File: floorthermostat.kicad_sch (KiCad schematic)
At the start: 29 parts, among them J1 Temp sensor socket 3 pin, J2 spi7segdisp, J3 Conn_01x06_Socket, J5 Programmin connector, Q1 BC549, SW1 Reset pushbutton, SW2 Enable pushbutton, U1 ESP32-WROOM-32, U2 GOLD 240V 3A SSR, U3 BD33FC0FP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

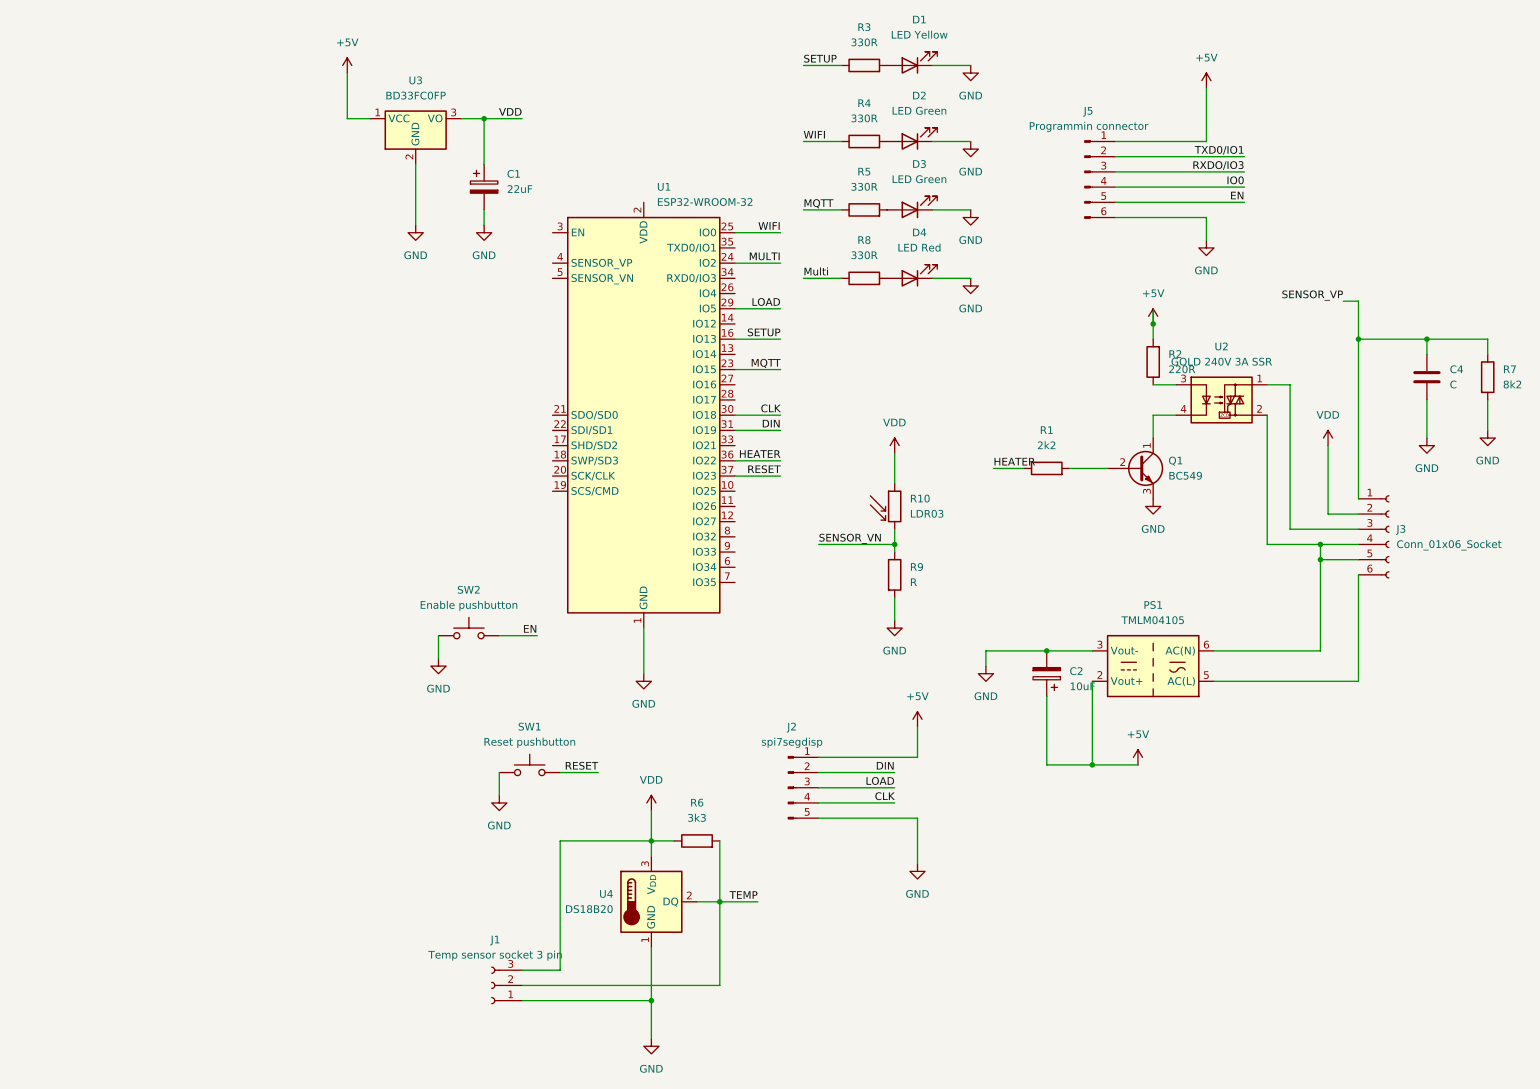
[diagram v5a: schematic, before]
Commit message: Checked all the component footprints.
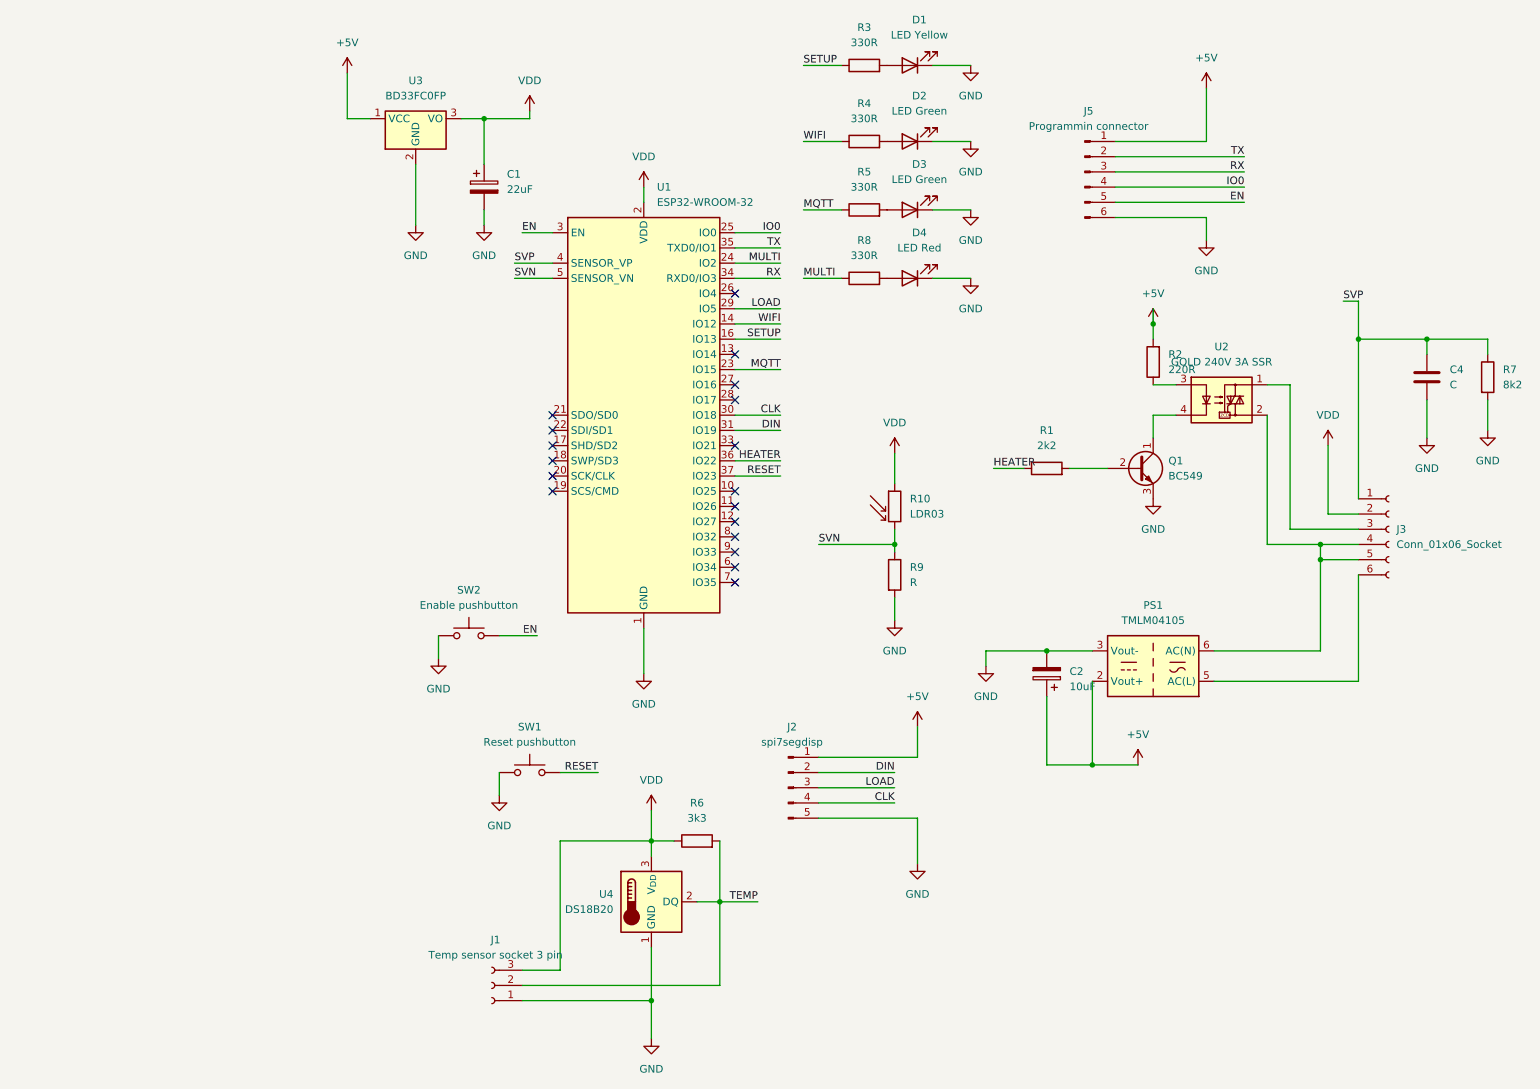
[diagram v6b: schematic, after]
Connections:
- net Multi is gone; now on net MULTI: R8.1
- net RXDO/IO3 is gone; now on net RX: J5.3 (Pin_3)
- net SENSOR_VN is gone; now on net SVN: R10.2, R9.1
- net SENSOR_VP is gone; now on net SVP: C4.1, J3.1 (Pin_1), R7.1
- net TXD0/IO1 is gone; now on net TX: J5.2 (Pin_2)
- net EN: now also U1.3 (EN)
- net IO0: now also U1.25 (IO0)
- net VDD: now also U1.2 (VDD)
- net WIFI: now also U1.14 (IO12); no longer U1.25 (IO0)
- net RX: now reaches U1.34 (RXD0/IO3)
- net TX: now reaches U1.35 (TXD0/IO1)
- net SVP: now reaches U1.4 (SENSOR_VP)
- net SVN: now reaches U1.5 (SENSOR_VN)
- no-connect marks 0 -> 18

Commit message: Started designing the pcb.
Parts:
- R2, R3, R4, R5, R6, R7, R8, R9: footprint Resistor_THT:R_Axial_DIN0207_L6.3mm_D2.5mm_P2.54mm_Vertical -> Resistor_THT:R_Axial_DIN0207_L6.3mm_D2.5mm_P15.24mm_Horizontal
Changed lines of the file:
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@@
 			)
 		)
-		(property "Footprint" "Resistor_THT:R_Axial_DIN0207_L6.3mm_D2.5mm_P2.54mm_Vertical"
+		(property "Footprint" "Resistor_THT:R_Axial_DIN0207_L6.3mm_D2.5mm_P15.24mm_Horizontal"
 			(at 149.86 23.368 90)
 			(effects
@@
 			)
 		)
-		(property "Footprint" "Resistor_THT:R_Axial_DIN0207_L6.3mm_D2.5mm_P2.54mm_Vertical"
+		(property "Footprint" "Resistor_THT:R_Axial_DIN0207_L6.3mm_D2.5mm_P15.24mm_Horizontal"
 			(at 149.86 58.928 90)
 			(effects
@@
 			)
 		)
-		(property "Footprint" "Resistor_THT:R_Axial_DIN0207_L6.3mm_D2.5mm_P2.54mm_Vertical"
+		(property "Footprint" "Resistor_THT:R_Axial_DIN0207_L6.3mm_D2.5mm_P15.24mm_Horizontal"
 			(at 252.222 73.66 90)
 			(effects
@@
 			)
 		)
-		(property "Footprint" "Resistor_THT:R_Axial_DIN0207_L6.3mm_D2.5mm_P2.54mm_Vertical"
+		(property "Footprint" "Resistor_THT:R_Axial_DIN0207_L6.3mm_D2.5mm_P15.24mm_Horizontal"
 			(at 149.86 47.498 90)
 			(effects
@@
 			)
 		)
-		(property "Footprint" "Resistor_THT:R_Axial_DIN0207_L6.3mm_D2.5mm_P2.54mm_Vertical"
+		(property "Footprint" "Resistor_THT:R_Axial_DIN0207_L6.3mm_D2.5mm_P15.24mm_Horizontal"
 			(at 199.898 71.12 90)
 			(effects
@@
 			)
 		)
-		(property "Footprint" "Resistor_THT:R_Axial_DIN0207_L6.3mm_D2.5mm_P2.54mm_Vertical"
+		(property "Footprint" "Resistor_THT:R_Axial_DIN0207_L6.3mm_D2.5mm_P15.24mm_Horizontal"
 			(at 121.92 152.908 90)
 			(effects
@@
 			)
 		)
-		(property "Footprint" "Resistor_THT:R_Axial_DIN0207_L6.3mm_D2.5mm_P2.54mm_Vertical"
+		(property "Footprint" "Resistor_THT:R_Axial_DIN0207_L6.3mm_D2.5mm_P15.24mm_Horizontal"
 			(at 153.162 106.68 90)
 			(effects
@@
 			)
 		)
-		(property "Footprint" "Resistor_THT:R_Axial_DIN0207_L6.3mm_D2.5mm_P2.54mm_Vertical"
+		(property "Footprint" "Resistor_THT:R_Axial_DIN0207_L6.3mm_D2.5mm_P15.24mm_Horizontal"
 			(at 149.86 36.068 90)
 			(effects

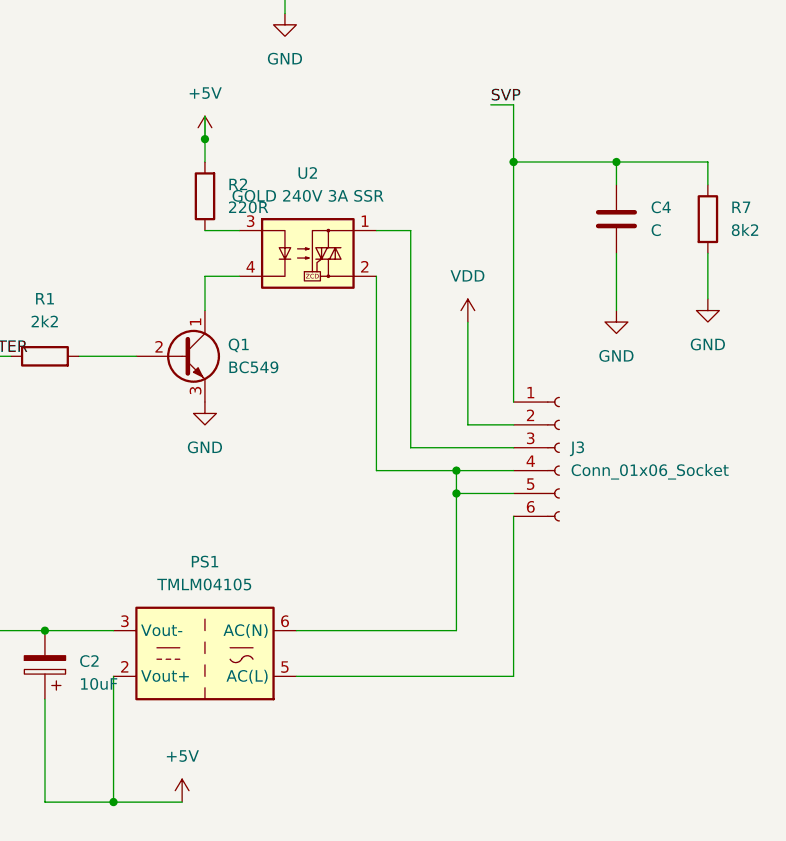
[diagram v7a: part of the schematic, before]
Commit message: Sketching component positions to pcb.
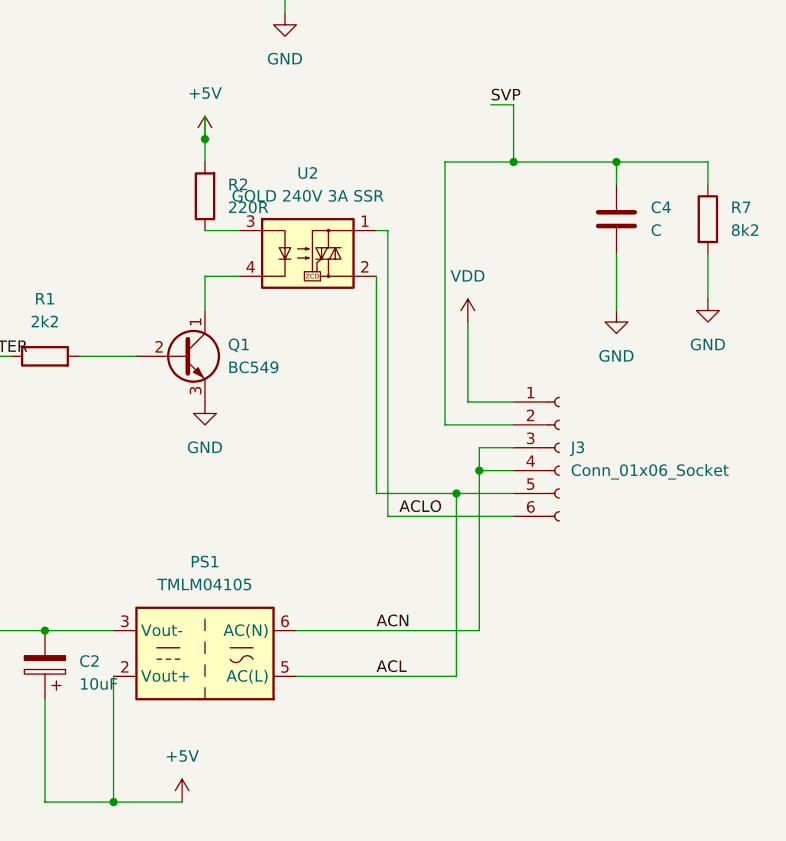
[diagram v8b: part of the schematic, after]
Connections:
- net SVP: now also J3.2 (Pin_2); no longer J3.1 (Pin_1)
- net VDD: now also J3.1 (Pin_1); no longer J3.2 (Pin_2)
- net ACLO: now reaches U2.1
- net ACLO: now also J3.6 (Pin_6); no longer J3.3 (Pin_3)
- net ACL: now reaches J3.5 (Pin_5), U2.2
- net ACL: now also PS1.5 (AC(L)); no longer J3.4 (Pin_4), PS1.6 (AC(N))
- new net ACN: J3.3 (Pin_3), J3.4 (Pin_4), PS1.6 (AC(N))
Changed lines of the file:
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@@
 	(paper "A4")
+	(junction
+		(at 114.3 177.8)
+		(diameter 0)
+		(color 0 0 0 0)
+	)
+	(junction
+		(at 86.36 30.48)
+		(diameter 0)
+		(color 0 0 0 0)
+	)
 	(junction
 		(at 232.41 67.31)
@@
 	)
 	(junction
-		(at 114.3 177.8)
+		(at 114.3 151.13)
+		(diameter 0)
+		(color 0 0 0 0)
+	)
+	(junction
+		(at 198.12 64.77)
+		(diameter 0)
+		(color 0 0 0 0)
+	)
+	(junction
+		(at 125.73 161.29)
 		(diameter 0)
 		(color 0 0 0 0)
@@
 	)
 	(junction
-		(at 86.36 30.48)
-		(diameter 0)
-		(color 0 0 0 0)
-	)
-	(junction
-		(at 114.3 151.13)
-		(diameter 0)
-		(color 0 0 0 0)
-	)
-	(junction
-		(at 226.06 101.6)
-		(diameter 0)
-		(color 0 0 0 0)
-	)
-	(junction
-		(at 198.12 64.77)
-		(diameter 0)
-		(color 0 0 0 0)
-	)
-	(junction
-		(at 125.73 161.29)
-		(diameter 0)
-		(color 0 0 0 0)
-	)
-	(junction
 		(at 243.84 67.31)
 		(diameter 0)
@@
 		(color 0 0 0 0)
 	)
+	(junction
+		(at 228.6 101.6)
+		(diameter 0)
+		(color 0 0 0 0)
+	)
 	(no_connect
 		(at 128.27 102.87)
@@
 	(wire
 		(pts
-			(xy 217.17 74.93) (xy 220.98 74.93)
+			(xy 218.44 74.93) (xy 217.17 74.93)
 		)
 		(stroke
@@
 	(wire
 		(pts
+			(xy 232.41 106.68) (xy 218.44 106.68)
+		)
+		(stroke
+			(width 0)
+			(type default)
+		)
+	)
+	(wire
+		(pts
 			(xy 142.24 137.16) (xy 158.75 137.16)
 		)
@@
 	(wire
 		(pts
+			(xy 208.28 119.38) (xy 228.6 119.38)
+		)
+		(stroke
+			(width 0)
+			(type default)
+		)
+	)
+	(wire
+		(pts
 			(xy 91.44 54.61) (xy 97.79 54.61)
 		)
@@
 	(wire
 		(pts
-			(xy 217.17 80.01) (xy 217.17 101.6)
+			(xy 226.06 124.46) (xy 208.28 124.46)
+		)
+		(stroke
+			(width 0)
+			(type default)
+		)
+	)
+	(wire
+		(pts
+			(xy 227.33 85.09) (xy 227.33 93.98)
+		)
+		(stroke
+			(width 0)
+			(type default)
+		)
+	)
+	(wire
+		(pts
+			(xy 217.17 104.14) (xy 217.17 80.01)
 		)
 		(stroke
@@
 	(wire
 		(pts
+			(xy 217.17 104.14) (xy 226.06 104.14)
+		)
+		(stroke
+			(width 0)
+			(type default)
+		)
+	)
+	(wire
+		(pts
 			(xy 191.77 34.29) (xy 207.01 34.29)
 		)
@@
 	(wire
 		(pts
-			(xy 227.33 96.52) (xy 232.41 96.52)
+			(xy 226.06 104.14) (xy 226.06 124.46)
 		)
 		(stroke
@@
 	(wire
 		(pts
+			(xy 228.6 99.06) (xy 228.6 101.6)
+		)
+		(stroke
+			(width 0)
+			(type default)
+		)
+	)
+	(wire
+		(pts
 			(xy 154.94 101.6) (xy 154.94 102.87)
 		)
@@
 	(wire
 		(pts
-			(xy 227.33 85.09) (xy 227.33 96.52)
-		)
-		(stroke
-			(width 0)
-			(type default)
-		)
-	)
-	(wire
-		(pts
 			(xy 170.18 121.92) (xy 170.18 119.38)
 		)
@@
 	(wire
 		(pts
+			(xy 232.41 67.31) (xy 224.79 67.31)
+		)
+		(stroke
+			(width 0)
+			(type default)
+		)
+	)
+	(wire
+		(pts
 			(xy 128.27 49.53) (xy 135.89 49.53)
 		)
@@
 	(wire
 		(pts
-			(xy 208.28 124.46) (xy 232.41 124.46)
-		)
-		(stroke
-			(width 0)
-			(type default)
-		)
-	)
-	(wire
-		(pts
 			(xy 167.64 45.72) (xy 161.29 45.72)
 		)
@@
 	(wire
 		(pts
+			(xy 224.79 96.52) (xy 232.41 96.52)
+		)
+		(stroke
+			(width 0)
+			(type default)
+		)
+	)
+	(wire
+		(pts
 			(xy 93.98 29.21) (xy 93.98 30.48)
 		)
@@
 	(wire
 		(pts
-			(xy 232.41 67.31) (xy 232.41 93.98)
+			(xy 218.44 106.68) (xy 218.44 74.93)
 		)
 		(stroke
@@
 	(wire
 		(pts
-			(xy 217.17 101.6) (xy 226.06 101.6)
-		)
-		(stroke
-			(width 0)
-			(type default)
-		)
-	)
-	(wire
-		(pts
 			(xy 187.96 124.46) (xy 187.96 138.43)
 		)
@@
 	(wire
 		(pts
+			(xy 232.41 104.14) (xy 226.06 104.14)
+		)
+		(stroke
+			(width 0)
+			(type default)
+		)
+	)
+	(wire
+		(pts
 			(xy 86.36 30.48) (xy 86.36 38.1)
 		)
@@
 	(wire
 		(pts
+			(xy 232.41 99.06) (xy 228.6 99.06)
+		)
+		(stroke
+			(width 0)
+			(type default)
+		)
+	)
+	(wire
+		(pts
+			(xy 228.6 101.6) (xy 228.6 119.38)
+		)
+		(stroke
+			(width 0)
+			(type default)
+		)
+	)
+	(wire
+		(pts
 			(xy 128.27 72.39) (xy 135.89 72.39)
 		)
@@
 	(wire
 		(pts
-			(xy 226.06 101.6) (xy 226.06 104.14)
-		)
-		(stroke
-			(width 0)
-			(type default)
-		)
-	)
-	(wire
-		(pts
 			(xy 128.27 67.31) (xy 135.89 67.31)
 		)
@@
 	(wire
 		(pts
+			(xy 224.79 67.31) (xy 224.79 96.52)
+		)
+		(stroke
+			(width 0)
+			(type default)
+		)
+	)
+	(wire
+		(pts
 			(xy 243.84 67.31) (xy 232.41 67.31)
 		)
@@
 	(wire
 		(pts
-			(xy 232.41 124.46) (xy 232.41 106.68)
-		)
-		(stroke
-			(width 0)
-			(type default)
-		)
-	)
-	(wire
-		(pts
-			(xy 220.98 99.06) (xy 232.41 99.06)
-		)
-		(stroke
-			(width 0)
-			(type default)
-		)
-	)
-	(wire
-		(pts
 			(xy 191.77 36.83) (xy 213.36 36.83)
 		)
@@
 	(wire
 		(pts
-			(xy 220.98 74.93) (xy 220.98 99.06)
-		)
-		(stroke
-			(width 0)
-			(type default)
-		)
-	)
-	(wire
-		(pts
 			(xy 191.77 46.99) (xy 207.01 46.99)
 		)
@@
 	(wire
 		(pts
-			(xy 208.28 119.38) (xy 226.06 119.38)
-		)
-		(stroke
-			(width 0)
-			(type default)
-		)
-	)
-	(wire
-		(pts
 			(xy 128.27 52.07) (xy 135.89 52.07)
 		)
@@
 	(wire
 		(pts
-			(xy 226.06 104.14) (xy 232.41 104.14)
+			(xy 227.33 93.98) (xy 232.41 93.98)
 		)
 		(stroke
@@
 	(wire
 		(pts
-			(xy 226.06 119.38) (xy 226.06 104.14)
+			(xy 232.41 101.6) (xy 228.6 101.6)
 		)
 		(stroke
@@
 		(pts
 			(xy 82.55 30.48) (xy 86.36 30.48)
-		)
-		(stroke
-			(width 0)
-			(type default)
-		)
-	)
-	(wire
-		(pts
-			(xy 226.06 101.6) (xy 232.41 101.6)
 		)
 		(stroke
@@
 		)
 	)
+	(label "ACN"
+		(at 217.17 119.38 0)
+		(fields_autoplaced yes)
+		(effects
+			(font
+				(size 1.27 1.27)
+			)
+			(justify left bottom)
+		)
+	)
+	(label "ACLO"
+		(at 219.71 106.68 0)
+		(fields_autoplaced yes)
+		(effects
+			(font
+				(size 1.27 1.27)
+			)
+			(justify left bottom)
+		)
+	)
 	(label "EN"
 		(at 213.36 44.45 180)
@@
 		)
 	)
+	(label "ACL"
+		(at 217.17 124.46 0)
+		(fields_autoplaced yes)
+		(effects
+			(font
+				(size 1.27 1.27)
+			)
+			(justify left bottom)
+		)
+	)
